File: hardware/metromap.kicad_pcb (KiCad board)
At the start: 4 copper layers, 100 x 100 mm, 171 parts, among them J1 USB_C_Receptacle_USB2.0_16P, U1 AZ1117-3.3, U2 SN74AHCT1G125DBVR, U3 ESP32-C6-MINI-1-H4, U4 CH221K, U5 VEML7700-TR

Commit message: added buttons
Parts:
- added C60: 1u, Capacitor_SMD:C_0603_1608Metric, B.Cu at (82.5, 108.5)
- added R13: 10k, Resistor_SMD:R_0603_1608Metric, F.Cu at (43.6, 116.3)
- added R14: 10k, Resistor_SMD:R_0603_1608Metric, F.Cu at (47.5, 125.3)
- added SW1: XUNPU_TS-1088-AR02016, metro-tracker:TS-1088-AR02016, B.Cu at (79.3, 109.2)
- added SW2: XUNPU_TS-1088-AR02016, metro-tracker:TS-1088-AR02016, B.Cu at (67.0, 115.0)
- R1: value 0R -> 10k
- moved R1 4.57 mm to (82.5, 105.5), turned to -90 degrees
- moved F1 3.30 mm to (87.5, 109.8)
- moved C11 1.31 mm to (80.2, 102.2)
- moved C12 1.31 mm to (82.4, 102.2)
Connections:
- net Net-(U3-EN) renamed /EN
- C14 pad 1: +5V -> +3.3V
- R2 pad 1: +5V -> +3.3V
- U2 pad 5: +5V -> +3.3V
- U3 pad 22: unconnected-(U3-IO8-Pad22) -> Net-(U3-IO8)
- U3 pad 23: unconnected-(U3-IO9-Pad23) -> Net-(U3-IO9)
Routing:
- net +5V: track 193.3 -> 189.1 mm, vias 104 -> 103
- net /EN: track 1.91 -> 0.00 mm
- net +3.3V: track 117.8 -> 117.9 mm, vias 0 -> 1

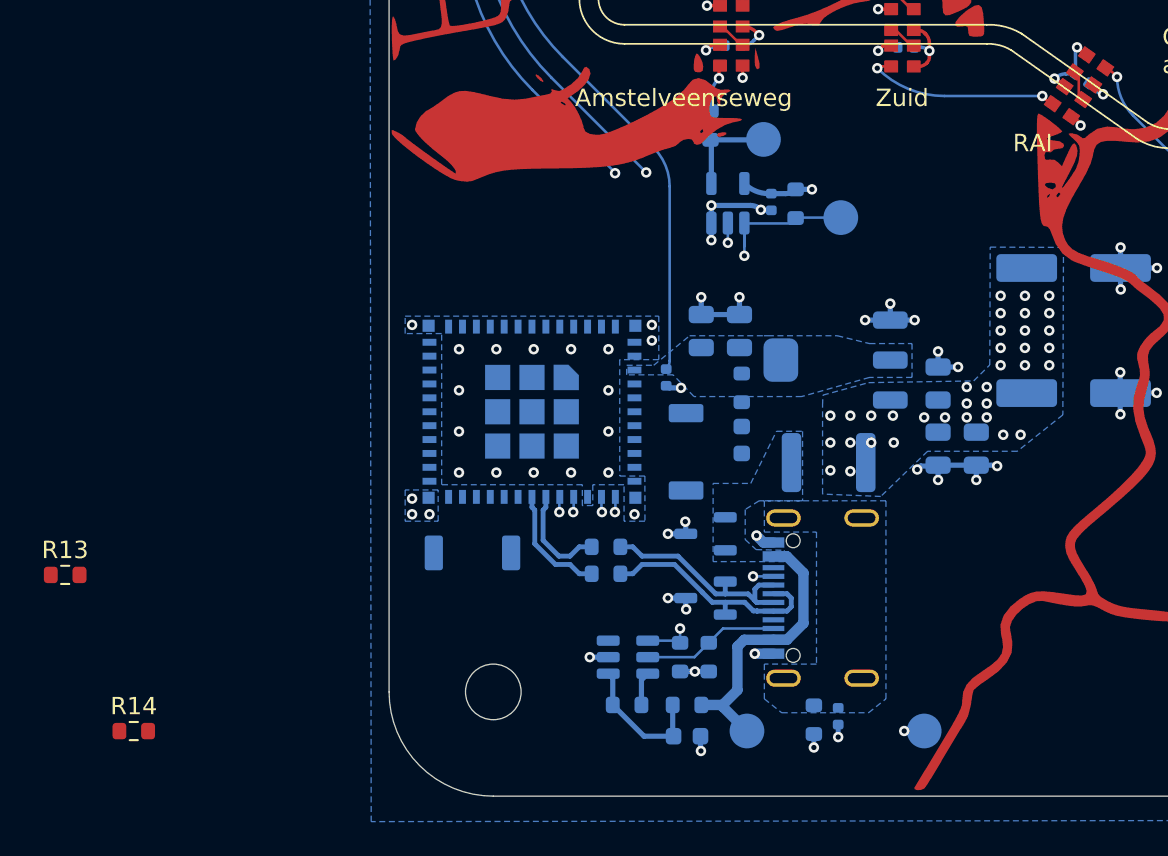
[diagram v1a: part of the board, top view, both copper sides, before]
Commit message: Added backup LDO and fixed OE ref
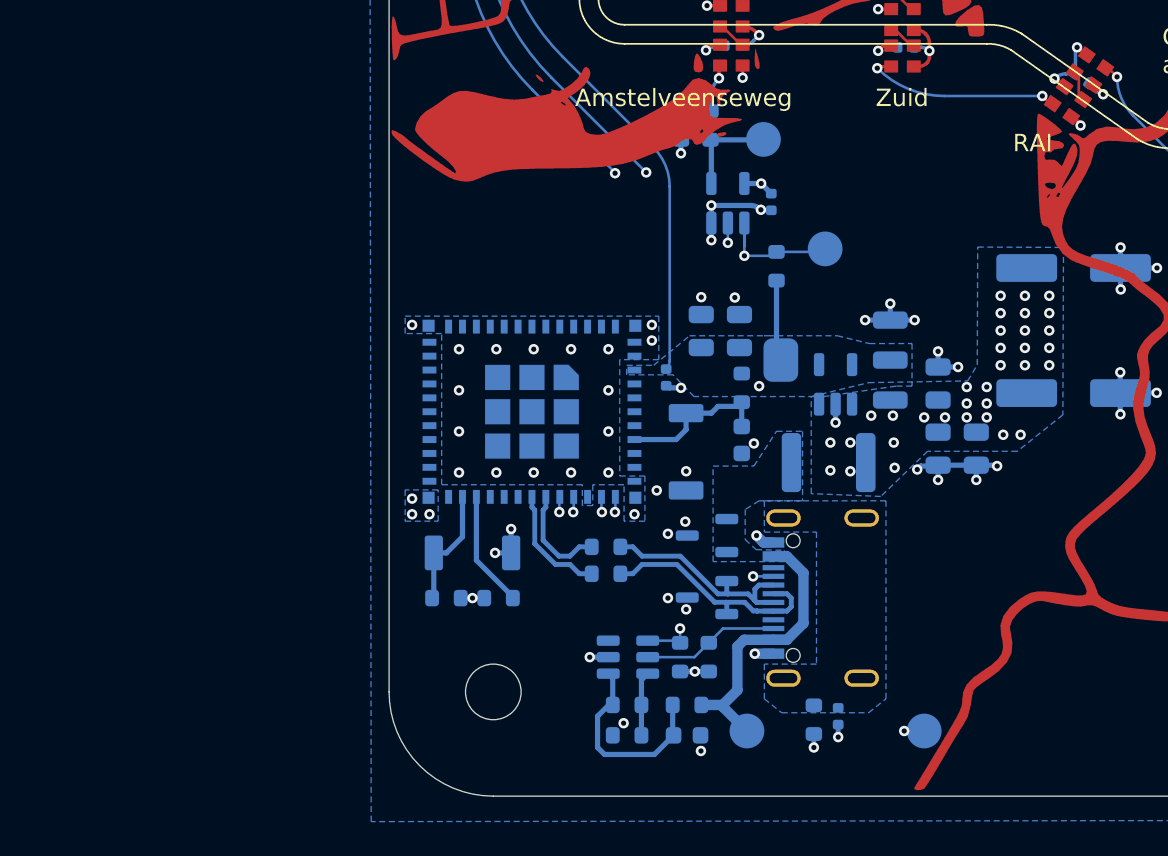
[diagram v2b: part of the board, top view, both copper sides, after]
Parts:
- added R15: 10k, Resistor_SMD:R_0603_1608Metric, B.Cu at (75.9, 125.5)
- added R16: 10k, Resistor_SMD:R_0603_1608Metric, B.Cu at (79.0, 90.4)
- added U6: AP2112K-3.3, Package_TO_SOT_SMD:SOT-23-5, B.Cu at (87.9, 105.3)
- D1, D2: value ESDA5V3L -> PSM712-LF-T7
- F1: footprint Fuse:Fuse_1812_4532Metric -> metro-tracker:Fuse_1812_4532Metric
- R13, R14: moved to B.Cu
- R6: value 0R -> 33R
- moved R13 25.0 mm to (68.5, 117.6)
- moved R14 19.6 mm to (65.5, 117.6), turned to 180 degrees
- moved R2 3.76 mm to (84.5, 98.5), turned to 90 degrees
- moved TP4 2.01 mm to (87.3, 97.5)
- moved D1 0.13 mm to (80.5, 114.0)
- moved D2 0.09 mm to (80.5, 117.6)
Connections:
- C14 pad 1: +3.3V -> +5V
- U2 pad 5: +3.3V -> +5V
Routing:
- net +3.3V: track 117.9 -> 142.3 mm, vias 1 -> 2
- net /EN: track 0.00 -> 9.02 mm
- net Net-(U3-IO9): track 0.00 -> 6.97 mm
- net Net-(U3-IO8): track 0.00 -> 6.69 mm
- net GND: track 161.4 -> 156.7 mm, vias 145 -> 153
- net Net-(U4-VDD): track 7.98 -> 11.7 mm
- net +5V: track 189.1 -> 190.9 mm, vias 103 -> 102
- net Net-(U4-CFG): track 1.95 -> 3.70 mm
- net /LEDs/DATA_IN: track 2.76 -> 4.46 mm
- net /~{OE}: track 27.8 -> 26.9 mm
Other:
- board text added: "B"
- board text added: "R"
- board text removed: "PATCH ANTENNA"

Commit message: fix tvs diodes
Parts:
- removed D2: PSM712-LF-T7, Package_TO_SOT_SMD:SOT-23-3
- added U7: SRV05-4, Package_TO_SOT_SMD:SOT-23-6, B.Cu at (80.0, 117.4)
- D1: value PSM712-LF-T7 -> P6SMB6.8CA/TR13; footprint Package_TO_SOT_SMD:SOT-23-3 -> Diode_SMD:D_SMB
- moved D1 20.2 mm to (94.6, 99.5), turned to 90 degrees
- moved C5 4.23 mm to (93.0, 109.4), turned to -90 degrees
- moved R7 2.34 mm to (75.9, 118.2)
- moved R5 2.30 mm to (75.9, 116.6)
- moved C10 1.26 mm to (95.0, 109.4)
- moved C9 1.08 mm to (97.0, 109.4)
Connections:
- D1 pad 1: /VBUS -> +5V
- D1 pad 2: /VBUS -> GND
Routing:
- net GND: track 156.7 -> 149.4 mm, vias 153 -> 165
- net /CON_USB_D-: track 12.7 -> 7.98 mm
- net /CON_USB_D+: track 13.6 -> 8.91 mm
- net /VBUS: track 16.4 -> 20.4 mm, vias 0 -> 2
- net /USB_D-: track 5.96 -> 8.03 mm
- net /USB_D+: track 6.76 -> 8.83 mm
